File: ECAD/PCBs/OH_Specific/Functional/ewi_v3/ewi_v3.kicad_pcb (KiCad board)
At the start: 2 copper layers, 96.1 x 78.8 mm, 43 parts, among them J1 BL IN, J2 BL OUT, J3 SW, SW1 FIRE, SW2 MC

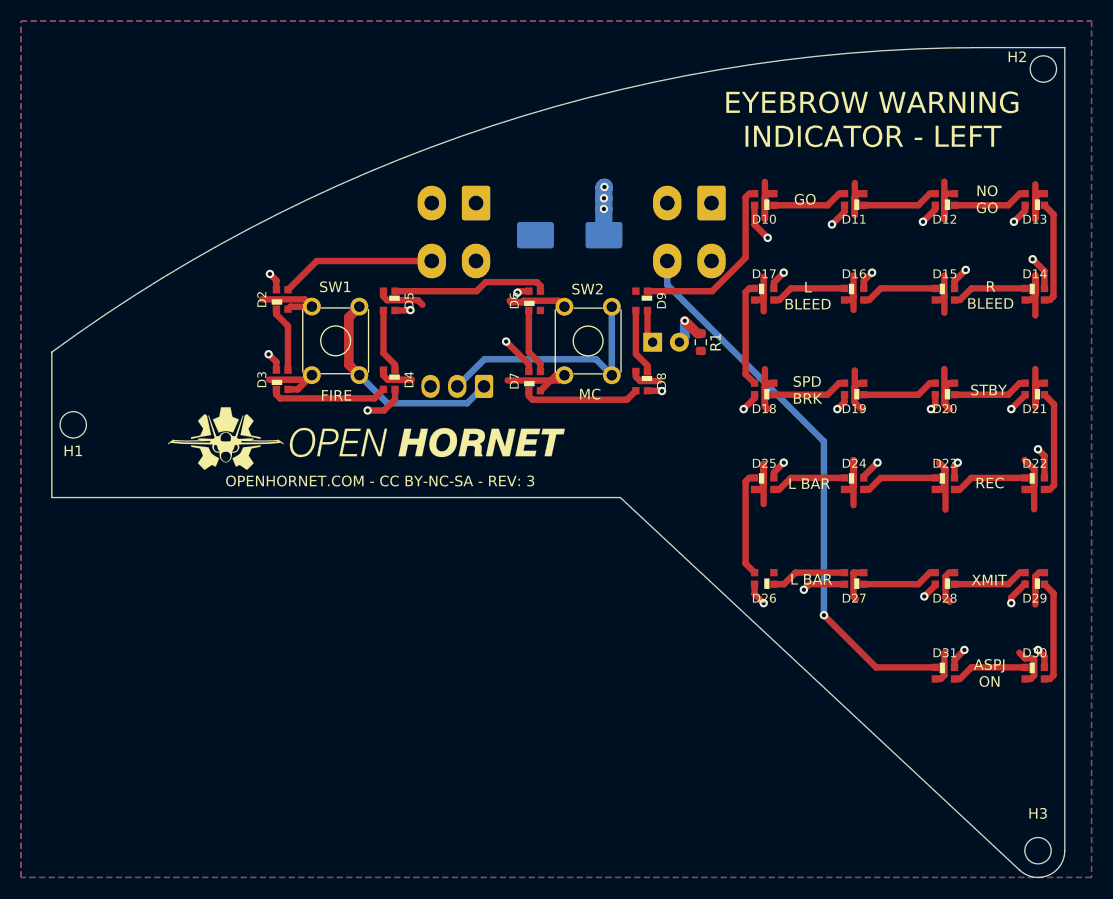
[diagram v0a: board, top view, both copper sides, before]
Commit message: EWI PCB Update
Added - 1000uF silkscreen
Added - Ready silkscreen
Changed - MC/APU Fire and Fire silkscreens down to remove collision with LEDs.
Changed - Silkscreen size and locations to match OH branding guidelines.
Changed - WS2812B-2020 LED footprint and schematic pin layout to match data sheet.
Changed - Revision from 3 to 4
Changed - Manufacturing files to match.
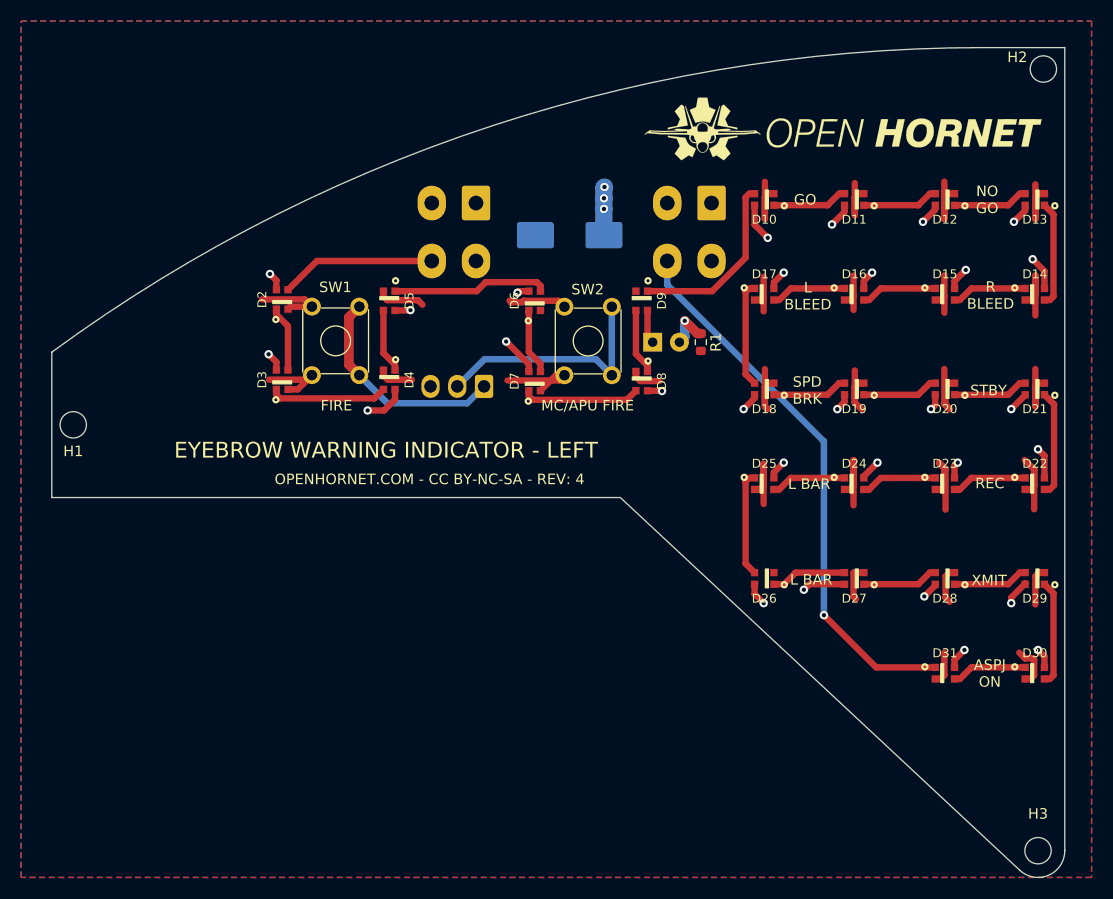
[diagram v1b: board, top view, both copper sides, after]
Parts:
- D10, D11, D12, D13, D14, D15, D16, D17, D18, D19, D2, D20, D21, D22, D23, D24, D25, D26, D27, D28, D29, D3, D30, D31, D4, D5, D6, D7, D8, D9: footprint KiCAD_Libraries:WS2812-2020 -> Openhornet:WS2812-2020
- SW2: value MC -> MC/APU FIRE
- moved G*** 54.0 mm to (176.7, 66.6)
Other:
- board text added: "1000uF"
- board text added: "OPENHORNET.COM - CC BY-NC-SA - REV: 4"
- board text added: "READY"
- board text removed: "OPENHORNET.COM - CC BY-NC-SA"
- board text removed: "OPENHORNET.COM - CC BY-NC-SA - REV: 3"
